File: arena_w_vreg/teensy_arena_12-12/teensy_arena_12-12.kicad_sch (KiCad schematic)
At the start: 0 parts

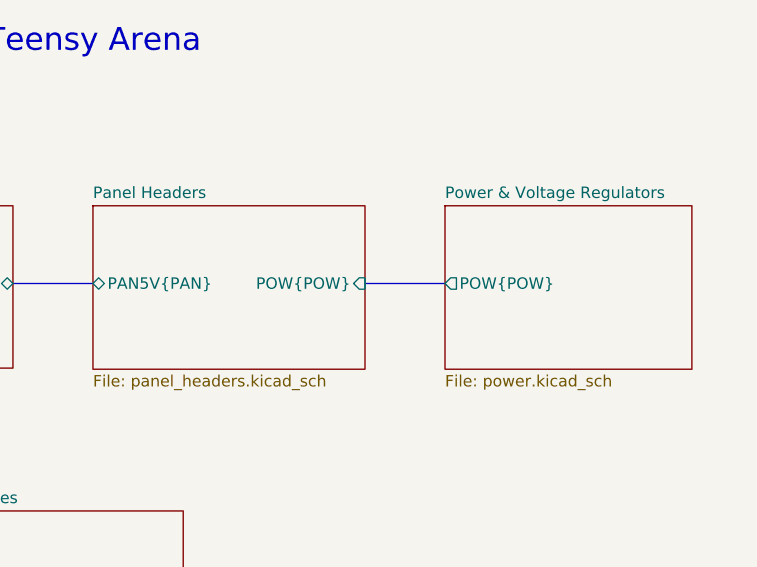
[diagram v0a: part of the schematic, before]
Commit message: Finished initial routing.
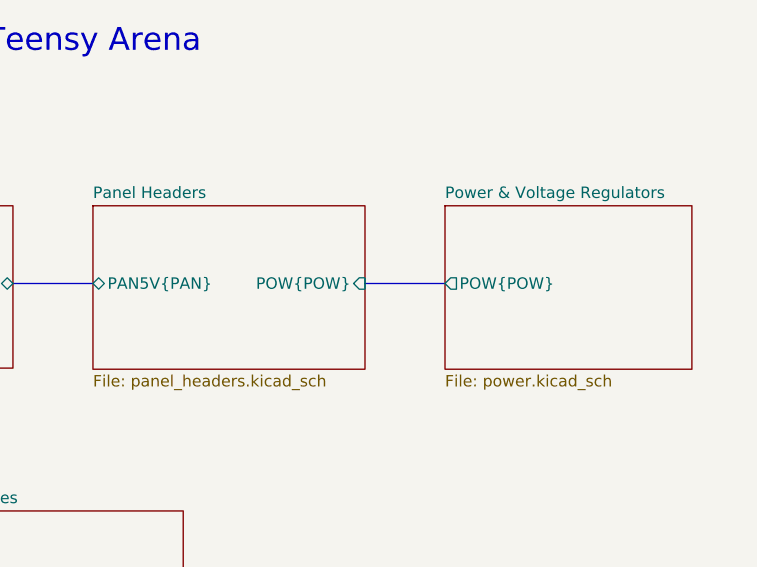
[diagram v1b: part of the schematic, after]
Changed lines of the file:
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@@
-    (stroke (width 0) (type default))
-  )
-  (bus (pts (xy 166.497 58.42) (xy 175.26 58.42))
     (stroke (width 0) (type default))
   )
@@
     (stroke (width 0) (type default))
   )
+  (bus (pts (xy 166.37 58.42) (xy 175.26 58.42))
+    (stroke (width 0) (type default))
+  )
